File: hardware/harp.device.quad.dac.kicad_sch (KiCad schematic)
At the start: 0 parts

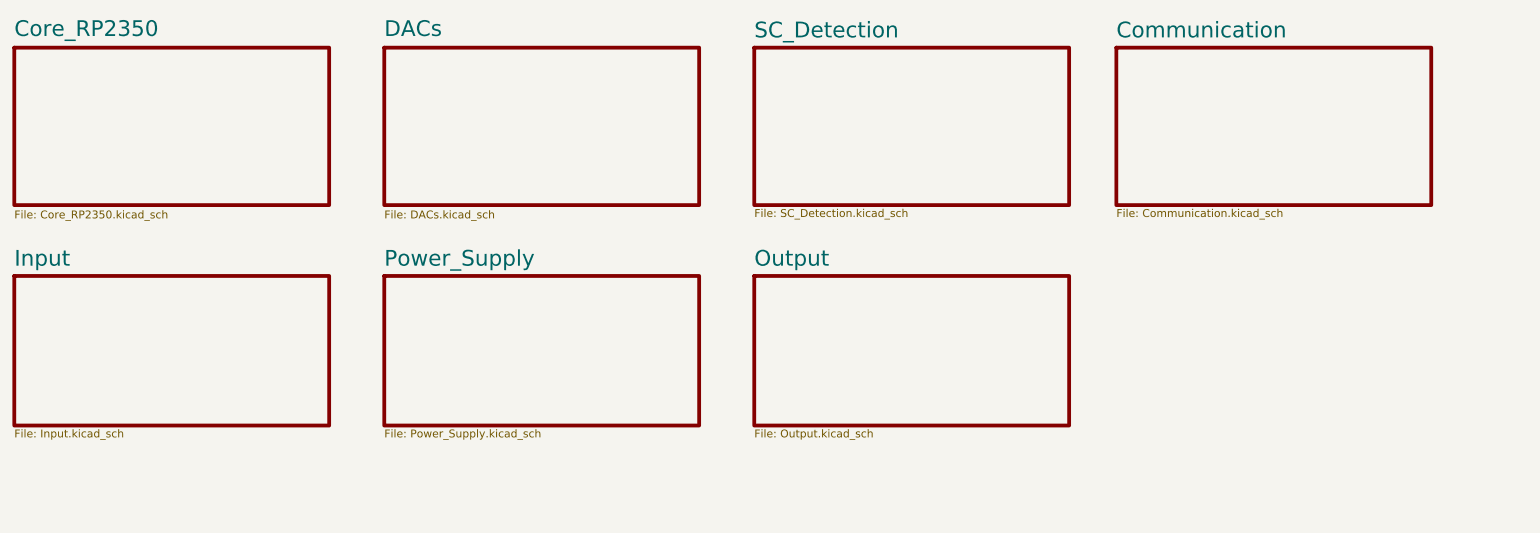
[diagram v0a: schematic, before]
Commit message: Added caps voltage rating + block diagram
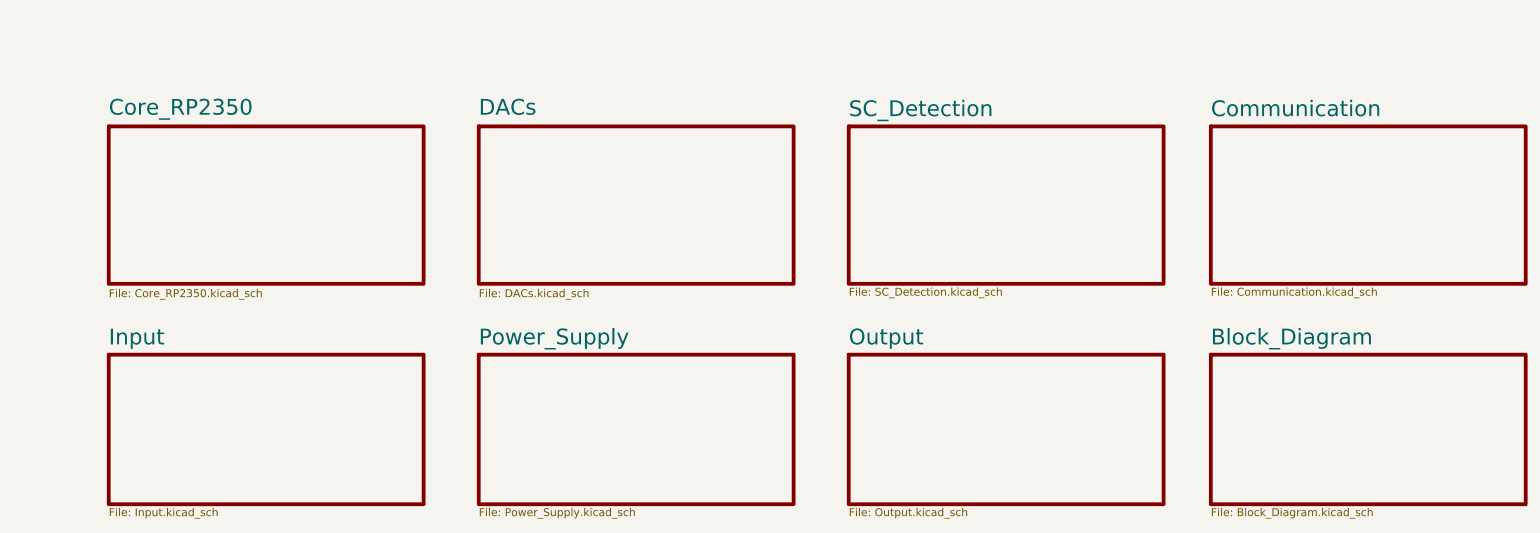
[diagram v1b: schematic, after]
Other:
- added sheet Block_Diagram (Block_Diagram.kicad_sch)
- title: Multi Channel HARP DAC -> harp device quad dac
